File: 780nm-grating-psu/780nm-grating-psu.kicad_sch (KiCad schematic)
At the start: 0 parts

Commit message: started psu sch
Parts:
- added C1: 100p, Capacitor_SMD:C_0402_1005Metric, symbol Device:C
- added C11, C12, C6: 4.7u, Capacitor_SMD:C_0603_1608Metric, symbol Device:C
- added C2: 22n, Capacitor_SMD:C_0402_1005Metric, symbol Device:C
- added C3, C5: 1u, Capacitor_SMD:C_0603_1608Metric, symbol Device:C
- added C4: 10u, Capacitor_SMD:C_0805_2012Metric, symbol Device:C
- added C7, C8: 22u, Capacitor_SMD:C_0603_1608Metric, symbol Device:C
- added C9: DNP, Capacitor_SMD:C_0402_1005Metric, symbol Device:C
- added D1: STTH1R04A, DIOM5126X265N, symbol STTH1R04A:STTH1R04A
- added L1: 1.5m, Inductor_SMD:L_Coilcraft_MSS1210H-XXX, symbol Device:L
- added Q1: FDD3N40TM, FDD3N40TM, symbol FDD3N40TM:FDD3N40TM
- added R1: 47k, Capacitor_SMD:C_0603_1608Metric, symbol Device:R
- added R10: 20k, Resistor_SMD:R_1206_3216Metric, symbol Device:R
- added R11: 16.2k, Resistor_SMD:R_1206_3216Metric, symbol Device:R
- added R2: 41.2k, Resistor_SMD:R_0603_1608Metric, symbol Device:R
- added R3: 34.8k, Resistor_SMD:R_0603_1608Metric, symbol Device:R
- added R4: 511k, Resistor_SMD:R_0603_1608Metric, symbol Device:R
- added R5: 0, Resistor_SMD:R_1206_3216Metric, symbol Device:R
- added R6: 0.3, Resistor_SMD:R_1206_3216Metric, symbol Device:R
- added R7, R8, R9: 511k, Resistor_SMD:R_1206_3216Metric, symbol Device:R
- added U1: LT3757AEDD, Package_DFN_QFN:DFN-10-1EP_3x3mm_P0.5mm_EP1.55x2.48mm, symbol Regulator_Switching:LT3757AEDD
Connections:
- new net: C1.1, R1.1, U1.1 (VC)
- new net: C3.1, U1.3 (SS)
- new net: R2.2, U1.4 (RT)
- new net: Q1.2 (S), R6.2, U1.6 (SENSE)
- new net: R5.1, U1.7 (GATE)
- new net: C6.2, U1.8 (INTVCC)
- new net: R3.2, R4.1, U1.9 (~{SHDN}/UVLO)
- new net: R7.2, R8.1
- new net: R8.2, R9.1
- new net: C2.1, C9.1, R1.2
- new net: Q1.1 (G), R5.2
- new net: D1.2 (A), L1.2, Q1.3 (D)
- new net: R10.1, R9.2
- new net +155V: C11.2, C12.2, C7.2, C8.2, D1.1 (K), R7.1
- new net +24V: C4.1, C5.1, L1.1, R4.2, U1.10 (VIN)
- new net FBX_+155V: R10.2, R11.1, U1.2 (FBX)
- new net GND: C1.2, C11.1, C12.1, C2.2, C3.2, C4.2, C5.2, C6.1, C7.1, C8.1, C9.2, R11.2, R2.1, R3.1, R6.1, U1.11 (GND), U1.5 (SYNC)
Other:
- note added: "+155V Boost Converter"

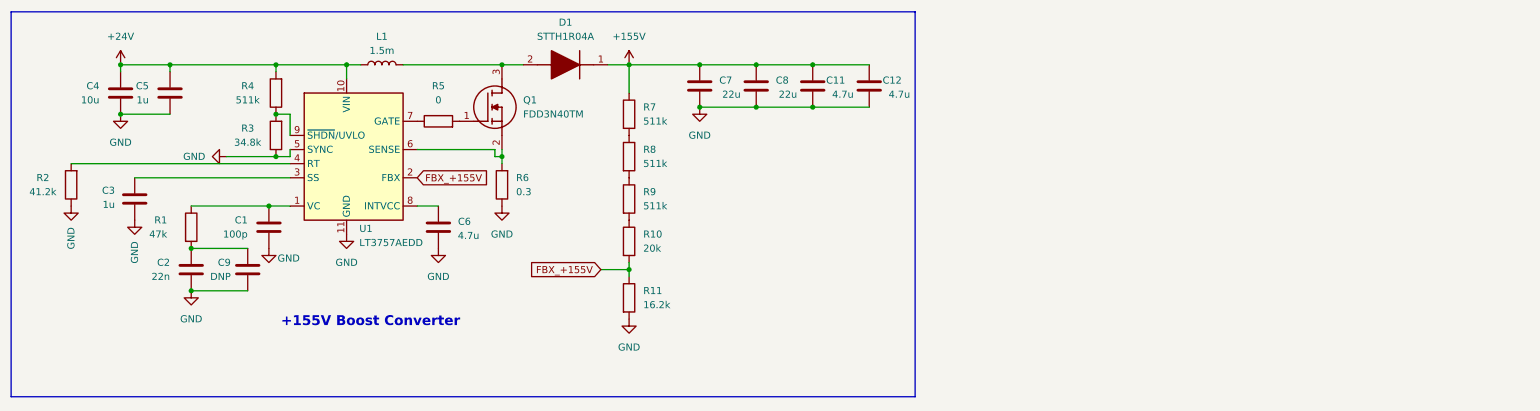
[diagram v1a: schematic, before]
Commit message: fixed vias
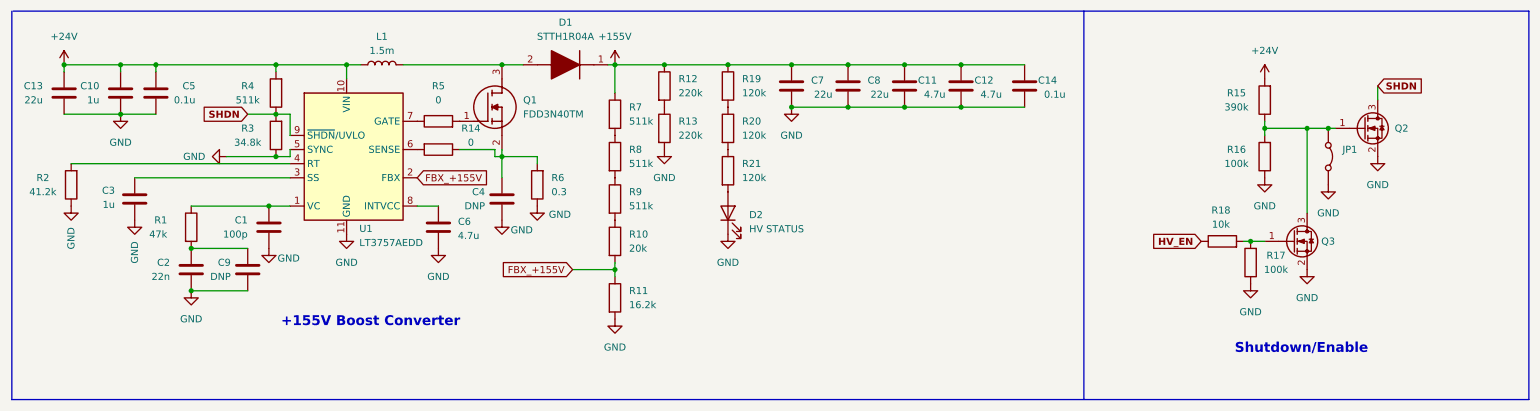
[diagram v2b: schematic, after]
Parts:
- added C10: 1u, Capacitor_SMD:C_0603_1608Metric, symbol Device:C
- added C13: 22u, Capacitor_SMD:C_1206_3216Metric, symbol Device:C
- added C14: 0.1u, Capacitor_SMD:C_0603_1608Metric, symbol Device:C
- added D2: HV STATUS, symbol Device:LED
- added JP1: Jumper_2_Bridged, symbol Jumper:Jumper_2_Bridged
- added Q2, Q3: 2N7002, Package_TO_SOT_SMD:SOT-23, symbol Transistor_FET:2N7002
- added R12, R13: 220k, Resistor_SMD:R_1206_3216Metric, symbol Device:R
- added R14: 0, Resistor_SMD:R_1206_3216Metric, symbol Device:R
- added R15: 390k, Resistor_SMD:R_0603_1608Metric, symbol Device:R
- added R16, R17: 100k, Resistor_SMD:R_0603_1608Metric, symbol Device:R
- added R18: 10k, Resistor_SMD:R_0603_1608Metric, symbol Device:R
- added R19, R20, R21: 120k, Resistor_SMD:R_1206_3216Metric, symbol Device:R
- C4: value 10u -> DNP; footprint Capacitor_SMD:C_0805_2012Metric -> Capacitor_SMD:C_0402_1005Metric
- C5: value 1u -> 0.1u
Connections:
- net +155V: now also C14.2, R12.1, R19.1
- net +24V: now also C10.1, C13.1, R15.2; no longer C4.1
- net GND: now also C10.2, C13.2, C14.1, D2.1 (K), JP1.2 (B), Q2.2 (S), Q3.2 (S), R13.2, R16.1, R17.1
- net at Q1.2 (S), R6.2: now also C4.1, R14.1; no longer U1.6 (SENSE)
- net SHDN: now reaches R3.2, R4.1, U1.9 (~{SHDN}/UVLO)
- net SHDN: now also Q2.3 (D)
- new net: R20.2, R21.1
- new net: D2.2 (A), R21.2
- new net: R14.2, U1.6 (SENSE)
- new net: R12.2, R13.1
- new net: JP1.1 (A), Q2.1 (G), Q3.3 (D), R15.1, R16.2
- new net: Q3.1 (G), R17.2, R18.2
- new net: R19.2, R20.1
- new net HV_EN: R18.1
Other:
- note added: "Shutdown/Enable"
- moved on the sheet: C11, C12, C5, C7, C8, R10, R11, R6, R7, R8, R9

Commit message: psu sch is complete
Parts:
- removed C14: 0.1u, Capacitor_SMD:C_0603_1608Metric, symbol Device:C
- removed C8: 22u, Capacitor_SMD:C_0603_1608Metric, symbol Device:C
- added C15, C16, C18, C19, C41: 4.7u, Capacitor_SMD:C_0603_1608Metric, symbol Device:C
- added C17, C26: 10n, Capacitor_SMD:C_0402_1005Metric, symbol Device:C
- added C20, C37: 10n, Capacitor_SMD:C_0603_1608Metric, symbol Device:C
- added C21: 22u, Capacitor_SMD:C_1206_3216Metric, symbol Device:C
- added C22, C25, C35: 1u, Capacitor_SMD:C_0603_1608Metric, symbol Device:C
- added C23, C36: 0.1u, Capacitor_SMD:C_0603_1608Metric, symbol Device:C
- added C24: 47n, Capacitor_SMD:C_0402_1005Metric, symbol Device:C
- added C27: 10u, Capacitor_SMD:C_0402_1005Metric, symbol Device:C
- added C28: 4.7u, Capacitor_SMD:C_0402_1005Metric, symbol Device:C
- added C29, C31: 22u, UCS2E220MPD:PCAP_10x20-THRU-ELECT_NCA, symbol Device:C_Polarized
- added C30: 0.1u, PHE426HA6100JR05:CAP_PHE426_AH_KEM, symbol Device:C
- added C33: 47u, Capacitor_SMD:C_1210_3225Metric, symbol Device:C
- added C34: 10u, Capacitor_SMD:C_0603_1608Metric, symbol Device:C
- added D3: ​​​STPS2H100A, Diode_SMD:D_SMA, symbol Device:D_Schottky
- added D4: SMBJ24CA-TR, Diode_SMD:D_SMB, symbol Diode:PTVS26VZ1USK
- added D5, D6, D7, D8: LED, LED_SMD:LED_0603_1608Metric, symbol Device:LED
- added F1: 0437001.WRA, symbol Device:Fuse
- added FB1: 1000 ohms, Inductor_SMD:L_0603_1608Metric, symbol Device:FerriteBead
- added IC1: ADP7142ARDZ-5.0-R7, SOIC127P600X175-9N, symbol ADP7142ARDZ-R7:ADP7142ARDZ-R7
- added IC2: LT8618EDDB#TRPBF, SON50P200X300X80-11N-D, symbol LT8618EDDB#TRPBF:LT8618EDDB#TRPBF
- added J1: TSW-102-07-G-D, HDRV4W64P254_2X2_508X508X838P, symbol TSW-102-07-G-D:TSW-102-07-G-D
- added J2: 1755736, 1755736:1755736, symbol 1755736:1755736
- added J3: 54-00166, 54-00166:CONN3_54-00166_TEN, symbol 54-00166:54-00166
- added J7: 1715747, 1715747:1715747, symbol 1715747:1715747
- added L2: 33u, symbol Device:L
- added R22: 39.9k, Resistor_SMD:R_0603_1608Metric, symbol Device:R
- added R23, R25: 49.9k, Resistor_SMD:R_0603_1608Metric, symbol Device:R
- added R24: 18.2k, Resistor_SMD:R_0603_1608Metric, symbol Device:R
- added R26: 1.02M, Resistor_SMD:R_0603_1608Metric, symbol Device:R
- added R27: 187k, Resistor_SMD:R_0603_1608Metric, symbol Device:R
- added R28: 0, Resistor_SMD:R_0603_1608Metric, symbol Device:R
- added R29: 10k, Resistor_SMD:R_0603_1608Metric, symbol Device:R
- added R30: 3.3k, Resistor_SMD:R_0603_1608Metric, symbol Device:R
- added R31: 1k, Resistor_SMD:R_0603_1608Metric, symbol Device:R
- added R32: 2.2k, Resistor_SMD:R_0603_1608Metric, symbol Device:R
- added R33: DNP, Resistor_SMD:R_1206_3216Metric, symbol Device:R
- added S1: 1101M2S3CQE2, 1101M2S3CQE2:SW_1101M2S3CQE2, symbol 1101M2S3CQE2:1101M2S3CQE2
- added TP3: +24V, TestPoint:TestPoint_Keystone_5015_Micro_Mini, symbol Connector:TestPoint
- added TP4: +9V, TestPoint:TestPoint_Keystone_5015_Micro_Mini, symbol Connector:TestPoint
- added TP5: +3.3V, TestPoint:TestPoint_Keystone_5015_Micro_Mini, symbol Connector:TestPoint
- added TP6: GND, TestPoint:TestPoint_Keystone_5015_Micro_Mini, symbol Connector:TestPoint
- added TP7: -5V, TestPoint:TestPoint_Keystone_5015_Micro_Mini, symbol Connector:TestPoint
- added TP8: +155V, TestPoint:TestPoint_Pad_D4.0mm, symbol Connector:TestPoint
- added U2: ADP7142ARDZ-3.3, Package_SO:SOIC-8-1EP_3.9x4.9mm_P1.27mm_EP2.29x3mm, symbol Regulator_Linear:ADP7142ARDZ-3.3
- C7: value 22u -> DNP; footprint Capacitor_SMD:C_0603_1608Metric -> Capacitor_SMD:C_1206_3216Metric
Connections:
- net +155V: now also C29.1, C30.1, C31.1, J2.1, TP8.1; no longer C7.2
- net +24V: now also C15.2, C18.2, C21.1, C22.1, C23.1, C35.1, C36.1, C37.1, C41.1, D5.2 (A), FB1.2, IC1.5 (EN), IC1.7 (VIN_1), IC1.8 (VIN_2), IC2.10 (VIN), IC2.9 (EN/UV), TP3.1, U2.5 (EN), U2.7 (VIN), U2.8 (VIN)
- net GND: now also C15.1, C16.1, C17.1, C18.1, C19.1, C20.1, C21.2, C27.2, C28.2, C29.2, C30.2, C31.2, C33.2, C34.2, C35.2, C36.2, C37.2, C41.2, D4.2 (A), IC1.4 (GND_1), IC1.9 (GND_2), J1.2, J1.3, J1.4, J2.2, J3.3 (C), J7.3, L2.2, R23.2, R25.2, R26.1, R28.1, R29.1, R30.1, R31.1, R32.1, R33.2, TP6.1, U2.4 (GND), U2.9 (GND); no longer C7.1
- net HV_EN: now also J1.1
- net G: now reaches Q1.1 (G), R5.2
- net at D1.2 (A), L1.2: now also C7.1, Q1.2 (S); no longer Q1.3 (D)
- net at C4.1, R14.1, R6.2: now also Q1.3 (D); no longer Q1.2 (S)
- new net: C7.2, R33.1
- new net: IC2.3 (BIAS), R28.2
- new net: C24.1, IC2.1 (BST)
- new net: C24.2, IC2.2 (SW), L2.1
- new net: C25.1, IC2.4 (INTVCC)
- new net: D8.2 (A), R32.2
- new net: C33.1, C34.1, D3.1 (K), D4.1 (K), FB1.1
- new net: D7.1 (K), R31.2
- new net: C17.2, U2.6 (SS)
- new net: IC1.3 (SENSE/ADJ), R22.2, R23.1
- new net: IC2.5 (RT), R24.1
- new net: D6.1 (K), R30.2
- new net: C20.2, IC1.6 (SS)
- new net: F1.1, J3.1 (A)
- new net: C26.2, IC2.7 (TR/SS)
- new net: D5.1 (K), R29.2
- new net +24V_RAW1: F1.2, S1.2
- new net +24V_RAW2: D3.2 (A), S1.3
- new net +3.3V: C16.2, D7.2 (A), J7.2, TP5.1, U2.1 (VOUT), U2.2 (VOUT), U2.3 (SENSE/ADJ)
- new net +9V: C19.2, D6.2 (A), IC1.1 (VOUT_1), IC1.2 (VOUT_2), J7.1, R22.1, TP4.1
- new net -5V: C22.2, C23.2, C25.2, C26.1, C27.1, C28.1, D8.1 (K), IC2.11 (GND), J7.4, R24.2, R27.2, TP7.1
- new net FB: IC2.6 (FB), R26.2, R27.1
- new net PG: IC2.8 (PG), R25.1
- no-connect marks 0 -> 2
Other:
- note added: "+155V output"
- note added: "+3.3V LDO"
- note added: "+9V LDO"
- note added: "-5V BUCK"
- note added: "Input Power Supply"
- note added: "Output (to PZT board)"
- note added: "PWR Status LEDs"
- note added: "RP GPIO"
- note added: "do NOT change the order of these pins!!!"
- moved on the sheet: C1, C10, C11, C12, C13, C2, C3, C4, C5, C6, C9, D1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

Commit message: footprints are all assigned
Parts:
- removed JP1: Jumper_2_Bridged, symbol Jumper:Jumper_2_Bridged
- added J4: TSW-102-07-G-S, TSW-102-07-G-S:TSW-102-XX-YY-S, symbol TSW-102-07-G-S:TSW-102-07-G-S
- D1: footprint DIOM5126X265N -> STTH1R04A:DIOM5126X265N
- D2: footprint (none) -> LED_SMD:LED_0603_1608Metric
- F1: footprint (none) -> Fuse:Fuse_1206_3216Metric
- IC1: footprint SOIC127P600X175-9N -> ADP7142ARDZ-R7:SOIC127P600X175-9N
- IC2: footprint SON50P200X300X80-11N-D -> LT8618EDDB#TRPBF:SON50P200X300X80-11N-D
- J1: footprint HDRV4W64P254_2X2_508X508X838P -> TSW-102-07-G-D:HDRV4W64P254_2X2_508X508X838P
- L2: footprint (none) -> Inductor_SMD_Wurth:L_Wurth_WE-LQSH-3012
- Q1: footprint FDD3N40TM -> FDD3N40TM:FDD3N40TM
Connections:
- net GND: now also J4.1
- net at Q2.1 (G), Q3.3 (D), R15.1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: now also J4.2

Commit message: layout 85% complete lol
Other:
- moved on the sheet: F1
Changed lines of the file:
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@@
 	)
 	(junction
-		(at 260.35 118.11)
-		(diameter 0)
-		(color 0 0 0 0)
-	)
-	(junction
 		(at 123.19 29.21)
 		(diameter 0)
@@
 	)
 	(junction
+		(at 261.62 118.11)
+		(diameter 0)
+		(color 0 0 0 0)
+	)
+	(junction
 		(at 104.14 142.24)
 		(diameter 0)
@@
 	(wire
 		(pts
+			(xy 261.62 118.11) (xy 262.89 118.11)
+		)
+		(stroke
+			(width 0)
+			(type default)
+		)
+	)
+	(wire
+		(pts
 			(xy 168.91 179.07) (xy 168.91 181.61)
 		)
@@
 	(wire
 		(pts
-			(xy 260.35 118.11) (xy 262.89 118.11)
-		)
-		(stroke
-			(width 0)
-			(type default)
-		)
-	)
-	(wire
-		(pts
 			(xy 31.75 38.1) (xy 38.1 38.1)
 		)
@@
 	(wire
 		(pts
+			(xy 261.62 118.11) (xy 260.35 118.11)
+		)
+		(stroke
+			(width 0)
+			(type default)
+		)
+	)
+	(wire
+		(pts
 			(xy 275.59 120.65) (xy 270.51 120.65)
 		)
@@
 	(wire
 		(pts
+			(xy 254 118.11) (xy 252.73 118.11)
+		)
+		(stroke
+			(width 0)
+			(type default)
+		)
+	)
+	(wire
+		(pts
 			(xy 25.4 96.52) (xy 36.83 96.52)
 		)
@@
 	(symbol
 		(lib_id "Device:Fuse")
-		(at 256.54 118.11 90)
+		(at 257.81 118.11 90)
 		(unit 1)
 		(body_style 1)
@@
 		(dnp no)
 		(property "Reference" "F1"
-			(at 257.81 122.936 90)
+			(at 259.08 122.936 90)
 			(show_name no)
 			(do_not_autoplace no)
@@
 		)
 		(property "Value" "0437001.WRA"
-			(at 257.81 125.476 90)
+			(at 259.08 125.476 90)
 			(show_name no)
 			(do_not_autoplace no)
@@
 		)
 		(property "Footprint" "Fuse:Fuse_1206_3216Metric"
-			(at 256.54 119.888 90)
+			(at 257.81 119.888 90)
 			(hide yes)
 			(show_name no)
@@
 		)
 		(property "Datasheet" ""
-			(at 256.54 118.11 0)
+			(at 257.81 118.11 0)
 			(hide yes)
 			(show_name no)
@@
 		)
 		(property "Description" "Fuse"
-			(at 256.54 118.11 0)
+			(at 257.81 118.11 0)
 			(hide yes)
 			(show_name no)
@@
 			)
 		)
-		(property "Datasheet" ""
+		(property "Datasheet" "MI0603J102R-10"
 			(at 231.14 93.98 0)
 			(hide yes)

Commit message: fixed hot loop
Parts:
- +155V TEST: renamed from TP8
- +24V TEST: renamed from TP3
- +3.3V TEST: renamed from TP5
- +9V TEST: renamed from TP4; value +9V -> +9V TEST
- -5V TEST: renamed from TP7
- C1, C10, C13, C15, C16, C17, C18, C19, C2, C21, C22, C23, C24, C25, C26, C3, C35, C36, C37, C4, C5, C6, C7, C9, D2, D5, D6, D7, D8, F1, FB1, R1, R10, R11, R12, R13, R14, R15, R16, R17, R18, R19, R2, R20, R21, R22, R23, R24, R25, R26, R27, R28, R29, R3, R30, R31, R32, R33, R4, R5, R6, R7, R8, R9: KiLib_Generator (none) -> SMD_2terminal_chip_molded
- C11, C12: value 4.7u -> 2.2u; footprint Capacitor_SMD:C_0603_1608Metric -> Capacitor_SMD:C_2220_5750Metric; KiLib_Generator (none) -> SMD_2terminal_chip_molded
- C20: footprint Capacitor_SMD:C_0603_1608Metric -> Capacitor_SMD:C_0402_1005Metric; KiLib_Generator (none) -> SMD_2terminal_chip_molded
- C27: footprint Capacitor_SMD:C_0402_1005Metric -> Capacitor_SMD:C_0805_2012Metric; KiLib_Generator (none) -> SMD_2terminal_chip_molded
- C28: footprint Capacitor_SMD:C_0402_1005Metric -> Capacitor_SMD:C_0603_1608Metric; KiLib_Generator (none) -> SMD_2terminal_chip_molded
- C30: footprint PHE426HA6100JR05:CAP_PHE426_AH_KEM -> Capacitor_SMD:C_1206_3216Metric; KiLib_Generator (none) -> SMD_2terminal_chip_molded
- C33: footprint Capacitor_SMD:C_1210_3225Metric -> Capacitor_SMD:C_2220_5750Metric; KiLib_Generator (none) -> SMD_2terminal_chip_molded
- C34: footprint Capacitor_SMD:C_0603_1608Metric -> Capacitor_SMD:C_1210_3225Metric; KiLib_Generator (none) -> SMD_2terminal_chip_molded
- C41: footprint Capacitor_SMD:C_0603_1608Metric -> Capacitor_SMD:C_0805_2012Metric; KiLib_Generator (none) -> SMD_2terminal_chip_molded
- IC GND TEST: renamed from TP6
- L1: KiLib_Generator (none) -> inductor/SMD
- Q2, Q3, U2: KiLib_Generator (none) -> package/gullwing
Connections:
- net Net-(U1-SENSE): now reaches C4.1, Q1.3 (D), R14.1, R6.2
